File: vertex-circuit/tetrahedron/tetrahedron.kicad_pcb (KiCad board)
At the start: 2 copper layers, 9 parts, among them J1 DIP-BLACK-MALE-HEADER-VERT_4P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, J2 DIP-BLACK-MALE-HEADER-VERT_4P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, J3 DIP-BLACK-MALE-HEADER-VERT_4P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, J4 DIP-BLACK-MALE-HEADER-VERT_4P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, J5 JACK-DC-005, J6 DIP-BLACK-MALE-HEADER-VERT_4P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, J7 DIP-BLACK-MALE-HEADER-VERT_4P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, J8 DIP-BLACK-MALE-HEADER-VERT_4P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

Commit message: save circuits
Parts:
- removed J2, J3, J7, J8: DIP-BLACK-MALE-HEADER-VERT_4P-2.54_, SeeedOPL-Connector-2016:H4-2.54
- moved J1 69.5 mm to (142.9, 51.4), turned to 90 degrees
- moved J6 62.8 mm to (142.9, 61.6), turned to 90 degrees
- moved J5 28.9 mm to (167.0, 61.6), turned to 90 degrees
- moved C1 27.3 mm to (120.0, 64.1), turned to 90 degrees
- moved J4 21.7 mm to (142.2, 72.4), turned to 90 degrees

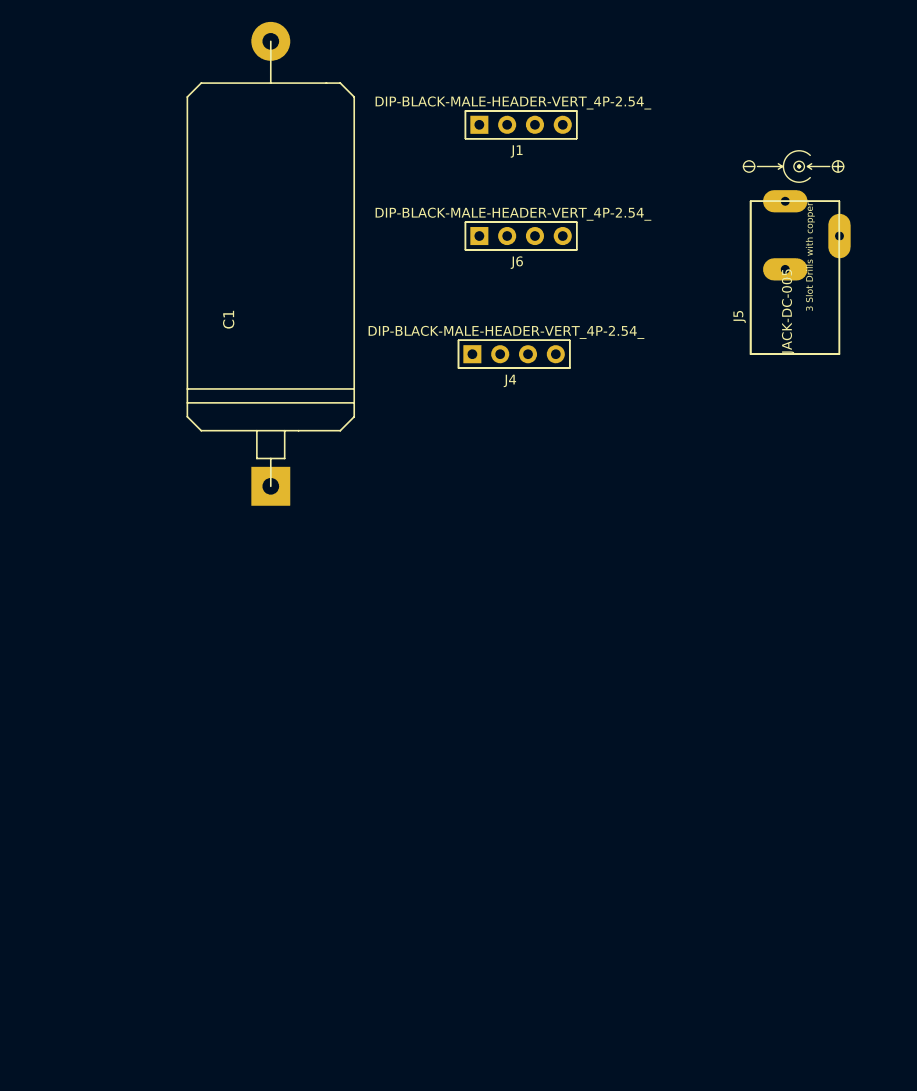
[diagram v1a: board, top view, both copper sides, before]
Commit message: shematic electrical problems were only warnings! move on to pcb
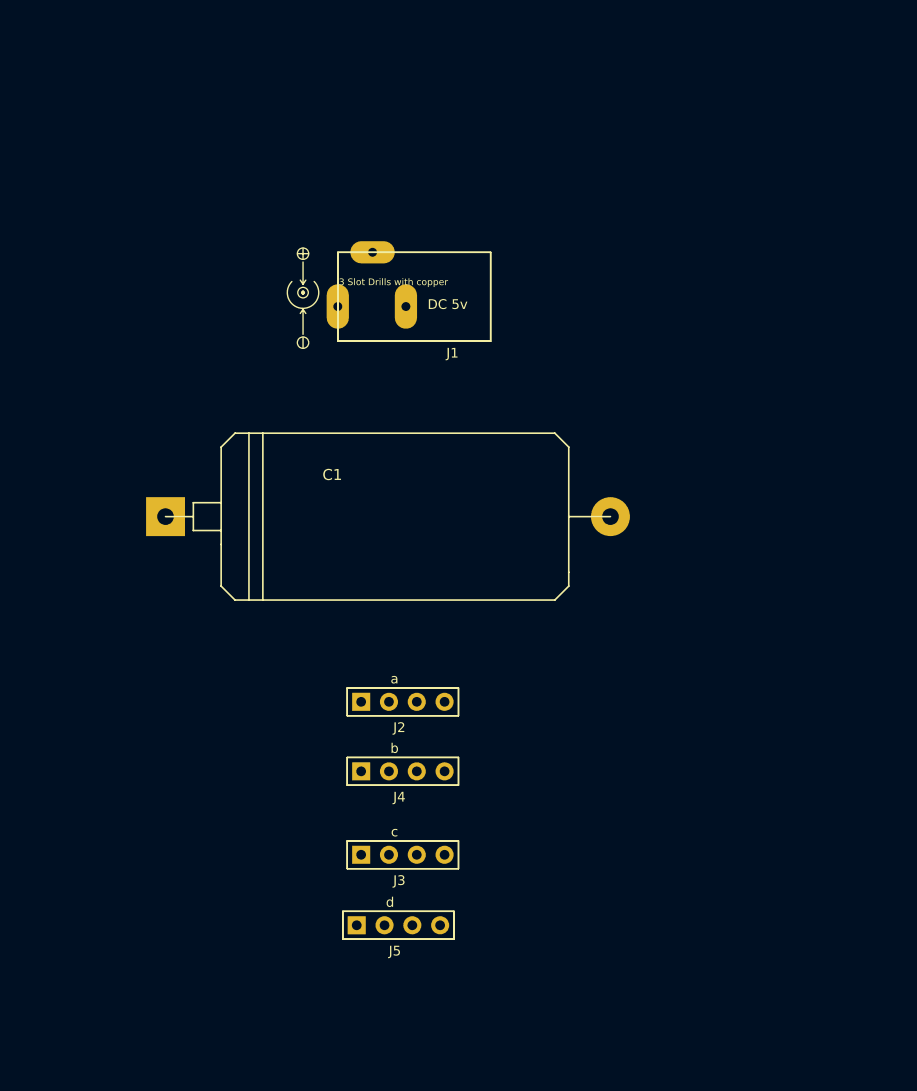
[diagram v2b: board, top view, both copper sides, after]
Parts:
- removed J6: DIP-BLACK-MALE-HEADER-VERT_4P-2.54_, SeeedOPL-Connector-2016:H4-2.54
- added J2: a, SeeedOPL-Connector-2016:H4-2.54, F.Cu at (132.1, 104.1)
- added J3: c, SeeedOPL-Connector-2016:H4-2.54, F.Cu at (132.1, 118.1)
- J1: value DIP-BLACK-MALE-HEADER-VERT_4P-2.54_ -> DC 5v; footprint SeeedOPL-Connector-2016:H4-2.54 -> SeeedOPL-Connector-2016:3P-L14.2_W11.0_H9.0MM
- J4: value DIP-BLACK-MALE-HEADER-VERT_4P-2.54_ -> b
- J5: value JACK-DC-005 -> d; footprint SeeedOPL-Connector-2016:3P-L14.2_W11.0_H9.0MM -> SeeedOPL-Connector-2016:H4-2.54
- moved J5 72.2 mm to (131.7, 124.5)
- moved J4 39.4 mm to (132.1, 110.5)
- moved C1 25.5 mm to (130.7, 87.2), turned to 0 degrees
- moved J1 21.4 mm to (129.3, 68.0), turned to 180 degrees
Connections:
- C1 pad 1: Net-(C1-Pad1) -> +5V
- C1 pad 2: Net-(C1-Pad2) -> GND
- J4 pad 1: Net-(J4-Pad1) -> +5V
- J4 pad 4: Net-(J4-Pad4) -> GND
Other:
- rule pad_to_mask_clearance: 0.2 -> 0

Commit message: circuity circuits
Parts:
- C1: footprint Discret:CP16 -> Discret:C1V8
- moved J5 44.1 mm to (144.2, 82.3), turned to 210 degrees
- moved J2 35.9 mm to (130.0, 68.3), turned to 270 degrees
- moved J4 33.1 mm to (114.3, 82.5), turned to 330 degrees
- moved J3 21.7 mm to (129.5, 96.5), turned to 270 degrees
- moved J1 20.4 mm to (136.4, 87.1), turned to 0 degrees
- moved C1 9.78 mm to (130.0, 77.5), turned to 180 degrees

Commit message: hey hey we can generate the entire circuit board meow!
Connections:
- J3 pad 1: +5V -> Net-(J3-Pad1)
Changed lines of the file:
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@@
 (kicad_pcb (version 4) (host pcbnew 4.0.7+dfsg1-1~bpo9+1)
   (general
-    (links 14)
-    (no_connects 14)
-    (area 110.396647 65.1034 148.137253 99.5775)
+    (links 13)
+    (no_connects 13)
+    (area 0 0 0 0)
     (thickness 1.6)
     (drawings 0)
@@
     (zones 0)
     (modules 6)
-    (nets 8)
+    (nets 9)
   )
   (page A4)
@@
   (net 6 "Net-(J3-Pad2)")
   (net 7 "Net-(J3-Pad3)")
+  (net 8 "Net-(J3-Pad1)")
   (net_class Default "This is the default net class."
     (clearance 0.2)
@@
     (add_net "Net-(J2-Pad2)")
     (add_net "Net-(J2-Pad3)")
+    (add_net "Net-(J3-Pad1)")
     (add_net "Net-(J3-Pad2)")
     (add_net "Net-(J3-Pad3)")
@@
     (fp_line (start -1.27 5.08) (end -1.27 -5.08) (layer F.SilkS) (width 0))
     (pad 1 thru_hole rect (at 0 -3.81 270) (size 1.651 1.651) (drill 0.889) (layers *.Cu *.Paste *.Mask)
-      (net 1 +5V))
+      (net 8 "Net-(J3-Pad1)"))
     (pad 2 thru_hole circle (at 0 -1.27 270) (size 1.651 1.651) (drill 0.889) (layers *.Cu *.Paste *.Mask)
       (net 6 "Net-(J3-Pad2)"))
